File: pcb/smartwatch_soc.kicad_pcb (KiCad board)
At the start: 2 copper layers, 31 parts, among them J2 USB_B_Micro, SW1 CK_KMS2xxGP, SW2 Button, SW3 Button, SW4 Button, SW5 Button, SW7 CK_KMS2xxGP, U1 MIC5219-3.3YM5, U2 LSM6DS3, U3 OLED_Display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

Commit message: pcb design
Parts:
- moved D1 29.5 mm to (148.7, 87.2), turned to 180 degrees
- moved R18 26.6 mm to (150.2, 84.6), turned to 180 degrees
- moved SW2 14.4 mm to (171.8, 79.5), turned to 90 degrees
- moved SW4 14.1 mm to (171.8, 71.5), turned to 90 degrees
- moved U3 14.0 mm to (140.1, 67.7), turned to 0 degrees
- moved C2 13.8 mm to (143.2, 72.1), turned to 0 degrees
- moved R12 11.2 mm to (170.8, 75.4), turned to 0 degrees
- moved R4 11.2 mm to (170.8, 83.4), turned to 0 degrees
- moved D10 11.0 mm to (155.9, 80.0)
- moved C3 10.5 mm to (145.7, 78.7)
- moved C4 10.5 mm to (148.2, 81.8)
- moved U1 10.5 mm to (151.9, 80.3)
- moved C1 10.3 mm to (148.8, 72.1), turned to 0 degrees
- moved C5 7.80 mm to (180.9, 67.1)
- moved SW1 7.36 mm to (144.7, 63.2)
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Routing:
- net VCC_3V3: track 0.00 -> 157.4 mm, vias 0 -> 8
- net ESP32_GPIO48: track 0.00 -> 30.8 mm, vias 0 -> 1
- net ESP32_GPIO34: track 0.00 -> 30.4 mm, vias 0 -> 1
- net ESP32_GPIO0: track 0.00 -> 22.4 mm
- net ESP32_GPIO37: track 0.00 -> 18.8 mm
- net ESP32_GPIO45: track 0.00 -> 17.9 mm
- net ESP32_GPIO18: track 0.00 -> 15.0 mm
- net ESP32_EN: track 0.00 -> 13.7 mm
- net ESP32_GPIO17: track 0.00 -> 13.2 mm
- net ESP32_GPIO16: track 0.00 -> 11.6 mm
- net ESP32_GPIO36: track 0.00 -> 11.5 mm
- net ESP32_GPIO38: track 0.00 -> 9.27 mm
- net VCC_5V: track 0.00 -> 6.46 mm
- net Net-(D1-A): track 0.00 -> 3.04 mm
- net VBUS: track 11.7 -> 8.74 mm
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- added copper zone on B.Cu, net GND
- added copper zone on F.Cu, net GND
- added copper zone on In1.Cu, net GND
- added copper zone on In2.Cu, net GND
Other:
- board outline added: 45.4 x 30.8 mm
- copper layers 2 -> 4

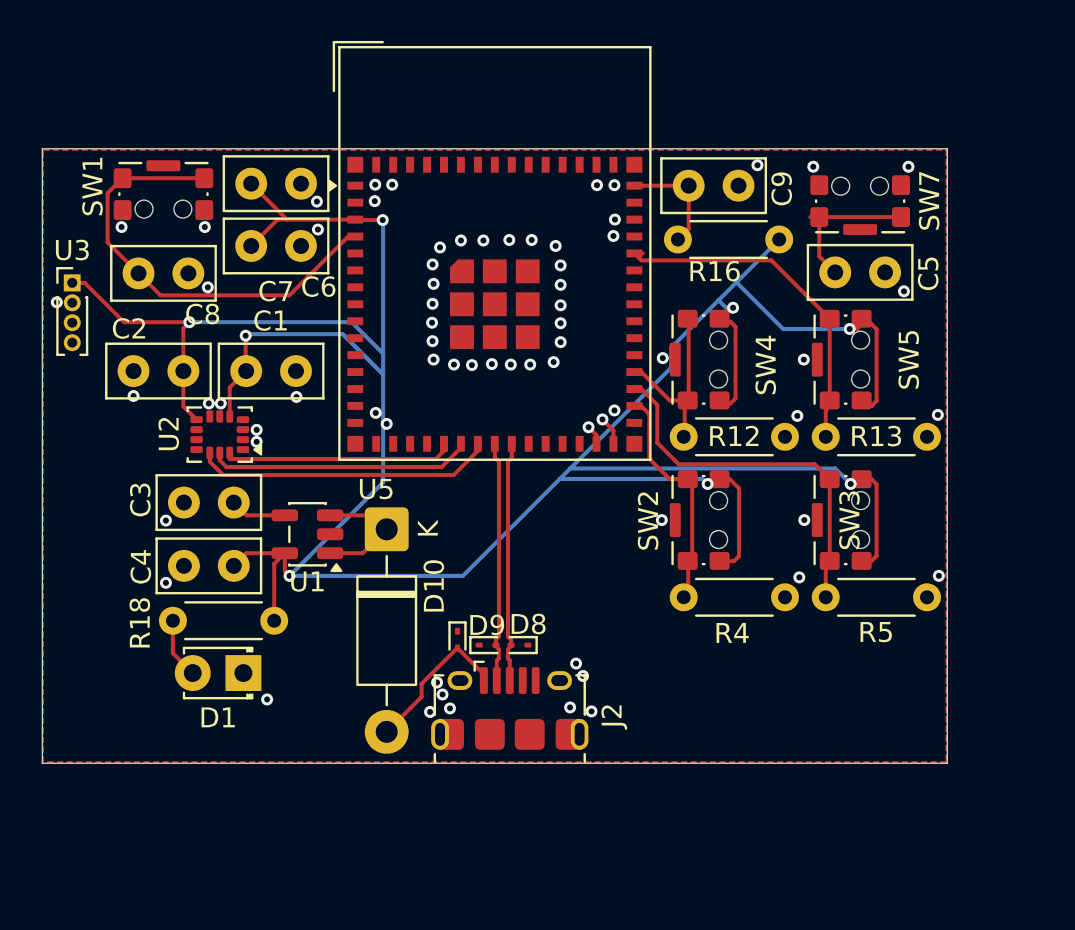
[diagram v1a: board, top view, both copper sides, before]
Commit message: pcb design rules
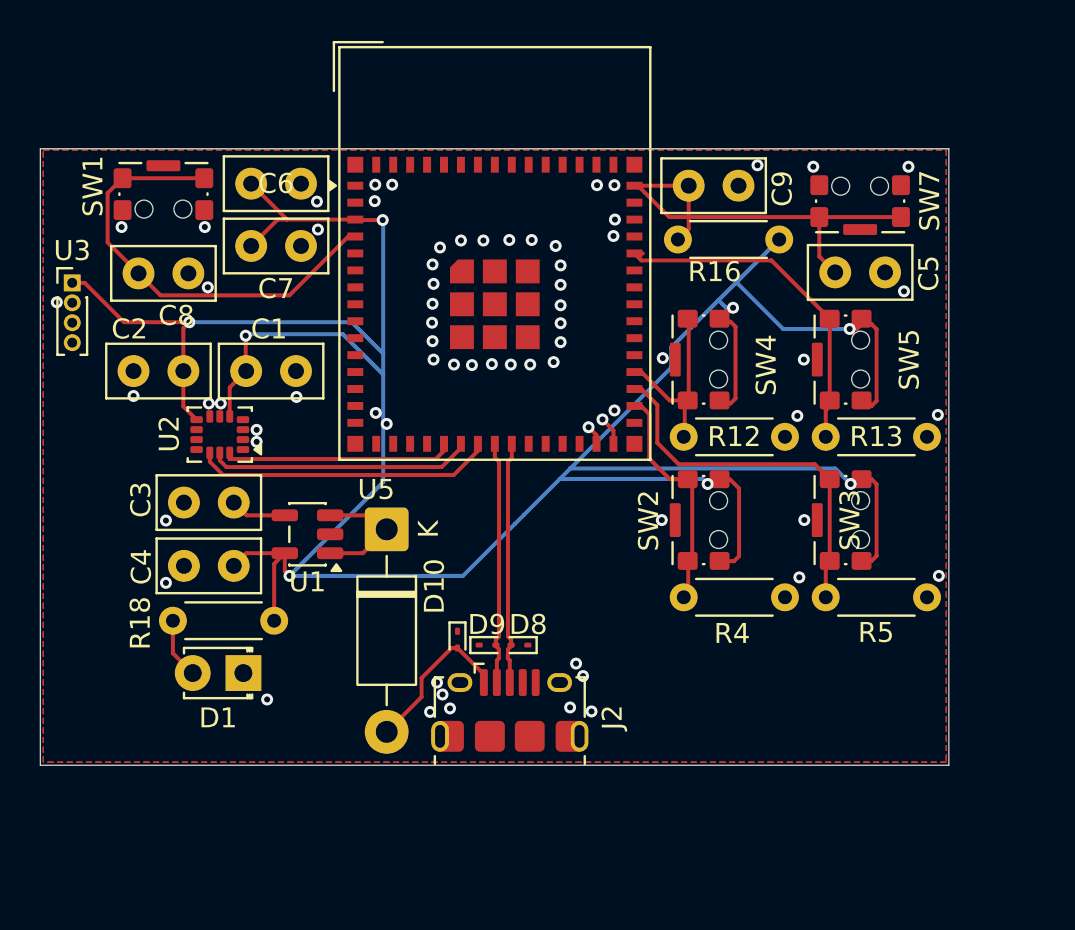
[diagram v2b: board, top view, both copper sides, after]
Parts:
- moved J2 0.10 mm to (162.1, 89.1)
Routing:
- net ESP32_EN: track 13.7 -> 23.2 mm
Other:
- board size 45.4 x 30.8 mm -> 45.6 x 30.9 mm
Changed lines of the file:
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@@
 		(tags "Diode SOD923")
 		(property "Reference" "D9"
-			(at -0.0334 -0.972 0)
+			(at -0.0334 -1.022 0)
 			(layer "F.SilkS")
 			(effects
@@
 		(tags "C Disc series Radial pin pitch 2.50mm diameter 5mm width 2.5mm Capacitor")
 		(property "Reference" "C7"
-			(at 1.25 2.3 0)
+			(at 1.25 2.15 0)
 			(layer "F.SilkS")
 			(effects
@@
 			(layer "F.Fab")
 		)
-		(fp_text user "${REFERENCE}"
-			(at 1.25 0 0)
-			(layer "F.Fab")
-			(effects
-				(font
-					(size 1 1)
-					(thickness 0.15)
-				)
-			)
-		)
 		(pad "1" thru_hole circle
 			(at 0 0)
@@
 		(tags "C Disc series Radial pin pitch 2.50mm diameter 5mm width 2.5mm Capacitor")
 		(property "Reference" "C6"
-			(at -0.9 -5.2 0)
+			(at 1.25 0 0)
 			(layer "F.SilkS")
 			(effects
@@
 			(layer "F.Fab")
 		)
-		(fp_text user "${REFERENCE}"
-			(at 1.25 0 0)
-			(layer "F.Fab")
-			(effects
-				(font
-					(size 1 1)
-					(thickness 0.15)
-				)
-			)
-		)
 		(pad "1" thru_hole circle
 			(at 0 0 180)
@@
 		(tags "C Disc series Radial pin pitch 2.50mm diameter 5mm width 2.5mm Capacitor")
 		(property "Reference" "C8"
-			(at -0.725 -2.075 0)
+			(at 0.6 -2.125 0)
 			(layer "F.SilkS")
 			(effects
@@
 		(tags "C Disc series Radial pin pitch 2.50mm diameter 5mm width 2.5mm Capacitor")
 		(property "Reference" "C1"
-			(at 1.25 -2.5 0)
+			(at 1.15 -2.1 0)
 			(layer "F.SilkS")
 			(effects
@@
 	(footprint "Connector_USB:USB_Micro-B_Amphenol_10118194-0001LF_Horizontal"
 		(layer "F.Cu")
-		(at 162.05 89)
+		(at 162.05 89.1)
 		(descr "USB Micro-B receptacle, horizontal, SMD, 10118194, 10118194-0001LF, 10118194-0002LF, 10118194-0101LF, 10118194-1001LF, https://cdn.amphenol-icc.com/media/wysiwyg/files/drawing/10118194.pdf")
 		(tags "USB Micro B horizontal SMD")
@@
 	)
 	(gr_rect
-		(start 138.6 60.925)
-		(end 184 91.75)
+		(start 138.5 60.925)
+		(end 184.075 91.85)
 		(stroke
 			(width 0.05)
@@
 	)
 	(segment
-		(start 177.125001 64.35)
+		(start 170.05 64.35)
 		(end 177.575 64.35)
 		(width 0.2)
@@
 	)
 	(segment
+		(start 168.3 62.775)
+		(end 168.475 62.775)
+		(width 0.2)
+		(layer "F.Cu")
+		(net 4)
+	)
+	(segment
+		(start 168.475 62.775)
+		(end 170.05 64.35)
+		(width 0.2)
+		(layer "F.Cu")
+		(net 4)
+	)
+	(segment
 		(start 177.575 64.35)
 		(end 181.675 64.35)
@@
 	)
 	(segment
-		(start 157.625 87.7675)
-		(end 157.625 88.425)
+		(start 155.875 89.5175)
+		(end 155.875 90.4)
 		(width 0.2)
 		(layer "F.Cu")
@@
 	)
 	(segment
-		(start 155.875 89.5175)
-		(end 155.875 90.4)
+		(start 159.1325 85.9675)
+		(end 157.625 87.475)
 		(width 0.2)
 		(layer "F.Cu")
@@
 	(segment
 		(start 159.425 85.9675)
-		(end 157.625 87.7675)
+		(end 159.1325 85.9675)
+		(width 0.2)
+		(layer "F.Cu")
+		(net 7)
+	)
+	(segment
+		(start 157.625 87.475)
+		(end 157.625 88.425)
 		(width 0.2)
 		(layer "F.Cu")

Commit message: pcb design rules progress
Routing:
- net VCC_3V3: track 157.4 -> 159.1 mm
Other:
- board size 45.6 x 30.9 mm -> 45.6 x 31 mm
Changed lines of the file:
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@@
 		(tags "Diode SOD923")
 		(property "Reference" "D9"
-			(at -0.0334 -1.022 0)
+			(at -0.0334 -1.097 0)
 			(layer "F.SilkS")
 			(effects
@@
 		(tags "Diode SOD923")
 		(property "Reference" "D8"
-			(at -0.4396 1.022 0)
+			(at -0.4396 1.072 0)
 			(layer "F.SilkS")
 			(effects
@@
 		(tags "Switch SPST KMS2")
 		(property "Reference" "SW3"
-			(at 0 0.225 90)
+			(at 0 3.1 90)
 			(layer "F.SilkS")
 			(effects
@@
 	(gr_rect
 		(start 138.5 60.925)
-		(end 184.075 91.85)
+		(end 184.075 91.93)
 		(stroke
 			(width 0.05)
@@
 	)
 	(segment
-		(start 179.460165 69.964835)
-		(end 179.7 69.725)
-		(width 0.2)
-		(layer "F.Cu")
-		(net 1)
-	)
-	(segment
 		(start 173.123999 68.9)
 		(end 172.575 69.448999)
@@
 	)
 	(segment
+		(start 180.199999 73.825)
+		(end 179.7 73.825)
+		(width 0.2)
+		(layer "F.Cu")
+		(net 1)
+	)
+	(segment
 		(start 140.725 67.65)
 		(end 142.7 69.625)
@@
 	)
 	(segment
-		(start 180.199999 77.5)
-		(end 179.7 77.5)
-		(width 0.2)
-		(layer "F.Cu")
-		(net 1)
-	)
-	(segment
-		(start 150.7625 81.2125)
-		(end 148.8375 81.2125)
+		(start 180.8 73.224999)
+		(end 180.199999 73.825)
 		(width 0.2)
 		(layer "F.Cu")
@@
 	)
 	(segment
-		(start 179.099999 69.964835)
-		(end 179.460165 69.964835)
+		(start 180.8 70.325001)
+		(end 180.8 73.224999)
 		(width 0.2)
 		(layer "F.Cu")
@@
 	)
 	(segment
-		(start 179.7 73.825)
-		(end 180.199999 73.825)
+		(start 180.199999 77.5)
+		(end 179.7 77.5)
 		(width 0.2)
 		(layer "F.Cu")
@@
 	)
 	(segment
-		(start 180.199999 73.825)
-		(end 180.451 73.573999)
+		(start 150.7625 81.2125)
+		(end 148.8375 81.2125)
 		(width 0.2)
 		(layer "F.Cu")
@@
 	)
 	(segment
-		(start 180.199999 69.725)
-		(end 179.7 69.725)
-		(width 0.2)
-		(layer "F.Cu")
-		(net 1)
-	)
-	(segment
 		(start 145.675 69.925)
 		(end 145.675 72.075)
@@
 	)
 	(segment
-		(start 180.451 73.573999)
-		(end 180.451 69.976001)
-		(width 0.2)
-		(layer "F.Cu")
-		(net 1)
-	)
-	(segment
 		(start 180.199999 81.6)
 		(end 180.451 81.348999)
@@
 	)
 	(segment
-		(start 180.451 69.976001)
-		(end 180.199999 69.725)
-		(width 0.2)
-		(layer "F.Cu")
-		(net 1)
-	)
-	(segment
 		(start 173.299999 81.6125)
 		(end 173.551 81.361499)
@@
 		(net 1)
 	)
+	(segment
+		(start 180.451 69.976001)
+		(end 180.8 70.325001)
+		(width 0.2)
+		(layer "F.Cu")
+		(net 1)
+	)
 	(via
 		(at 151 82.35)
@@
 	)
 	(via
-		(at 179.099999 69.964835)
+		(at 180.451 69.976001)
 		(size 0.6)
 		(drill 0.3)
@@
 	)
 	(segment
-		(start 155.7 64.525)
-		(end 155.675 64.5)
+		(start 171.805 68.52)
+		(end 172.52 68.52)
 		(width 0.2)
 		(layer "B.Cu")
@@
 	)
 	(segment
-		(start 155.7 72.25)
-		(end 155.7 71.2)
+		(start 172.52 68.52)
+		(end 173.17 67.87)
 		(width 0.2)
 		(layer "B.Cu")
@@
 	)
 	(segment
-		(start 173.42 67.62)
-		(end 175.764835 69.964835)
+		(start 155.7 64.525)
+		(end 155.675 64.5)
 		(width 0.2)
 		(layer "B.Cu")
@@
 	)
 	(segment
-		(start 179.07738 69.964835)
-		(end 179.08869 69.953525)
+		(start 155.7 72.25)
+		(end 155.7 71.2)
 		(width 0.2)
 		(layer "B.Cu")
@@
 	)
 	(segment
-		(start 170.15 71.9)
-		(end 170.15 70.89)
-		(width 0.2)
-		(layer "B.Cu")
-		(net 1)
-	)
-	(segment
 		(start 164.5625 77.4875)
 		(end 171.722664 77.4875)
@@
 	)
 	(segment
-		(start 172.52 68.52)
+		(start 173.17 67.87)
 		(end 173.42 67.62)
 		(width 0.2)
@@
 	)
 	(segment
+		(start 174.1 68.8)
+		(end 179.825 68.8)
+		(width 0.2)
+		(layer "B.Cu")
+		(net 1)
+	)
+	(segment
+		(start 156.525 76.825)
+		(end 156.525 73.075)
+		(width 0.2)
+		(layer "B.Cu")
+		(net 1)
+	)
+	(segment
+		(start 151 82.35)
+		(end 156.525 76.825)
+		(width 0.2)
+		(layer "B.Cu")
+		(net 1)
+	)
+	(segment
 		(start 154.125 69.625)
 		(end 145.975 69.625)
@@
 	)
 	(segment
-		(start 165.0875 76.9625)
-		(end 170.15 71.9)
+		(start 173.17 67.87)
+		(end 174.1 68.8)
+		(width 0.2)
+		(layer "B.Cu")
+		(net 1)
+	)
+	(segment
+		(start 169.35 72.7)
+		(end 169.35 70.975)
 		(width 0.2)
 		(layer "B.Cu")
@@
 	)
 	(segment
-		(start 151 82.35)
-		(end 155.7 77.65)
+		(start 169.35 70.975)
+		(end 171.805 68.52)
 		(width 0.2)
 		(layer "B.Cu")
@@
 	)
 	(segment
-		(start 170.15 70.89)
-		(end 172.52 68.52)
+		(start 156.525 73.075)
+		(end 155.7 72.25)
 		(width 0.2)
 		(layer "B.Cu")
@@
 	)
 	(segment
-		(start 175.764835 69.964835)
-		(end 179.07738 69.964835)
+		(start 179.825 68.8)
+		(end 180.451 69.426)
 		(width 0.2)
 		(layer "B.Cu")
@@
 	)
 	(segment
-		(start 155.7 77.65)
-		(end 155.7 72.25)
+		(start 165.0875 76.9625)
+		(end 169.35 72.7)
 		(width 0.2)
 		(layer "B.Cu")
@@
 	)
 	(segment
+		(start 180.451 69.426)
+		(end 180.451 69.976001)
+		(width 0.2)
+		(layer "B.Cu")
+		(net 1)
+	)
+	(segment
 		(start 173.42 67.62)
 		(end 175.565 65.475)
@@
 	)
 	(via
-		(at 147.55 73.7)
+		(at 147.275 73.7)
 		(size 0.6)
 		(drill 0.3)
@@
 	)
 	(via
-		(at 152.425 64.975)
+		(at 152.7 65.125)
 		(size 0.6)
 		(drill 0.3)
@@
 	)
 	(via
-		(at 155.875 74.725)
+		(at 155.925 74.29311)
 		(size 0.6)
 		(drill 0.3)
@@
 	)
 	(via
-		(at 146.9 67.875)
+		(at 147.05 67.6)
 		(size 0.6)
 		(drill 0.3)
@@
 	)
 	(via
-		(at 169.725 71.425)
+		(at 169.95 71.5)
 		(size 0.6)
 		(drill 0.3)
@@
 	)
 	(via
-		(at 167.3 74.05)
+		(at 167.275 73.9)
 		(size 0.6)
 		(drill 0.3)
@@
 	)
 	(via
-		(at 146.75 64.85)
+		(at 146.675 64.9)
 		(size 0.6)
 		(drill 0.3)
@@
 	)
 	(via
-		(at 146.95 73.7)
+		(at 146.575 73.7)
 		(size 0.6)
 		(drill 0.3)
@@
 	)
 	(via
-		(at 183.575 82.35)
+		(at 183.15 82.2)
 		(size 0.6)
 		(drill 0.3)
@@
 	)
 	(via
-		(at 143.175 73.325)
+		(at 143.625 73.275)
 		(size 0.6)
 		(drill 0.3)
@@
 	)
 	(via
-		(at 155.325 74.175)
+		(at 155.200002 74.29311)
 		(size 0.6)
 		(drill 0.3)
@@
 	)
 	(via
-		(at 151.35 73.375)
+		(at 152.65 72.775)
 		(size 0.6)
 		(drill 0.3)
@@
 		(net 2)
 		(net_name "GND")
-		(layer "F.Cu")
-		(hatch edge 0.5)
-		(connect_pads yes
-			(clearance 0.1524)
-		)
-		(min_thickness 0.1524)
-		(filled_areas_thickness no)
-		(fill
-			(thermal_gap 0.5)
-			(thermal_bridge_width 0.5)
-			(island_removal_mode 1)
-			(island_area_min 9.999999)
-		)
-		(polygon
-			(pts
-				(xy 138.65 60.975) (xy 183.95 60.975) (xy 183.95 91.7) (xy 138.65 91.7)
-			)
-		)
-	)
-	(zone
-		(net 2)
-		(net_name "GND")
 		(layers "F.Cu" "B.Cu" "In1.Cu" "In2.Cu")
 		(hatch edge 0.5)
@@
 			(thermal_bridge_width 0.5)
 			(island_removal_mode 1)
-			(island_area_min 9.999999)
+			(island_area_min 9.999998)
 		)
 		(polygon
 			(pts
-				(xy 138.65 60.975) (xy 183.95 60.975) (xy 183.95 91.7) (xy 138.65 91.7)
+				(xy 138.65 61) (xy 183.95 60.975) (xy 183.95 91.7) (xy 138.65 91.7)
 			)
 		)

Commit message: no more design errors!
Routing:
- net VCC_3V3: track 159.1 -> 160.0 mm
- net ESP32_GPIO48: track 30.8 -> 31.4 mm
- net ESP32_GPIO34: track 30.4 -> 30.9 mm
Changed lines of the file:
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@@
+	)
+	(segment
+		(start 179.924999 69.45)
+		(end 180.451 69.976001)
+		(width 0.2)
+		(layer "F.Cu")
+		(net 1)
 	)
 	(segment
@@
 		(net 1)
 	)
+	(segment
+		(start 179.7 69.45)
+		(end 179.924999 69.45)
+		(width 0.2)
+		(layer "F.Cu")
+		(net 1)
+	)
 	(via
 		(at 151 82.35)
@@
 	)
 	(via
-		(at 149.35 75.025)
+		(at 149.55 74.975)
 		(size 0.6)
 		(drill 0.3)
@@
 	)
 	(via
-		(at 149.35 75.625)
+		(at 149.5 75.625)
 		(size 0.6)
 		(drill 0.3)
@@
 	)
 	(via
-		(at 146.675 64.9)
+		(at 146.725 65.05)
 		(size 0.6)
 		(drill 0.3)
@@
 	)
 	(via
-		(at 142.575 64.85)
+		(at 142.575 65.025)
 		(size 0.6)
 		(drill 0.3)
@@
 	)
 	(segment
-		(start 166.001936 74.89311)
+		(start 164.475 74.15)
+		(end 164.825 74.5)
+		(width 0.2)
+		(layer "F.Cu")
+		(net 24)
+	)
+	(segment
+		(start 164.825 74.5)
+		(end 165.608826 74.5)
+		(width 0.2)
+		(layer "F.Cu")
+		(net 24)
+	)
+	(segment
+		(start 165.608826 74.5)
 		(end 166.4 75.291174)
 		(width 0.2)
@@
 	)
 	(via
-		(at 166.001936 74.89311)
+		(at 164.475 74.15)
 		(size 0.6)
 		(drill 0.3)
@@
 	)
 	(segment
-		(start 144.276 71.61895)
-		(end 144.276 73.826)
+		(start 154.599002 74.05)
+		(end 150.151 74.05)
 		(width 0.2)
 		(layer "In1.Cu")
@@
 	)
 	(segment
-		(start 145.34311 74.89311)
-		(end 166.001936 74.89311)
+		(start 164.01711 73.69211)
+		(end 154.951059 73.69211)
 		(width 0.2)
 		(layer "In1.Cu")
@@
 	)
 	(segment
-		(start 140.1 69.65)
-		(end 142.30705 69.65)
+		(start 154.951059 73.69211)
+		(end 154.599002 74.044167)
 		(width 0.2)
 		(layer "In1.Cu")
@@
 	(segment
 		(start 142.30705 69.65)
-		(end 144.276 71.61895)
+		(end 140.1 69.65)
 		(width 0.2)
 		(layer "In1.Cu")
@@
 	)
 	(segment
-		(start 144.276 73.826)
-		(end 145.34311 74.89311)
+		(start 149.9 74.301)
+		(end 150.151 74.05)
 		(width 0.2)
 		(layer "In1.Cu")
@@
 	)
 	(segment
+		(start 144.276 73.826)
+		(end 144.751 74.301)
+		(width 0.2)
+		(layer "In1.Cu")
+		(net 24)
+	)
+	(segment
+		(start 148.949 74.523943)
+		(end 148.949 74.5)
+		(width 0.2)
+		(layer "In1.Cu")
+		(net 24)
+	)
+	(segment
+		(start 144.751 74.301)
+		(end 149.9 74.301)
+		(width 0.2)
+		(layer "In1.Cu")
+		(net 24)
+	)
+	(segment
+		(start 154.599002 74.044167)
+		(end 154.599002 74.05)
+		(width 0.2)
+		(layer "In1.Cu")
+		(net 24)
+	)
+	(segment
+		(start 144.276 71.61895)
+		(end 142.30705 69.65)
+		(width 0.2)
+		(layer "In1.Cu")
+		(net 24)
+	)
+	(segment
+		(start 164.475 74.15)
+		(end 164.01711 73.69211)
+		(width 0.2)
+		(layer "In1.Cu")
+		(net 24)
+	)
+	(segment
+		(start 144.276 73.826)
+		(end 144.276 71.61895)
+		(width 0.2)
+		(layer "In1.Cu")
+		(net 24)
+	)
+	(segment
 		(start 167.25 75.052091)
 		(end 167.25 75.725)
@@
 	)
 	(segment
-		(start 144.94411 75.49411)
-		(end 166.250879 75.49411)
+		(start 166.69969 75.045299)
+		(end 166.69969 74.501781)
 		(width 0.2)
 		(layer "In1.Cu")
@@
 	)
 	(segment
-		(start 166.250879 75.49411)
+		(start 165.519989 76.225)
 		(end 166.69969 75.045299)
 		(width 0.2)
@@
 	)
 	(segment
-		(start 166.69969 75.045299)
-		(end 166.69969 74.501781)
+		(start 140.1 70.65)
+		(end 145.675 76.225)
 		(width 0.2)
 		(layer "In1.Cu")
@@
 	)
 	(segment
-		(start 140.1 70.65)
-		(end 144.94411 75.49411)
+		(start 145.675 76.225)
+		(end 165.519989 76.225)
 		(width 0.2)
 		(layer "In1.Cu")
@@
 		(min_thickness 0.1524)
 		(filled_areas_thickness no)
-		(fill
+		(fill yes
 			(thermal_gap 0.5)
 			(thermal_bridge_width 0.5)
